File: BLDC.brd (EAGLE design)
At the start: 75.9 x 76.2 mm, 119 parts, among them J7 1-770178-0, J8 1-770174-1, U1 DRV8302, U102 LM3671MF-3.3/NOPB, U104 MCP2562, U2 STM32F405RGT6, Y1 8MHz

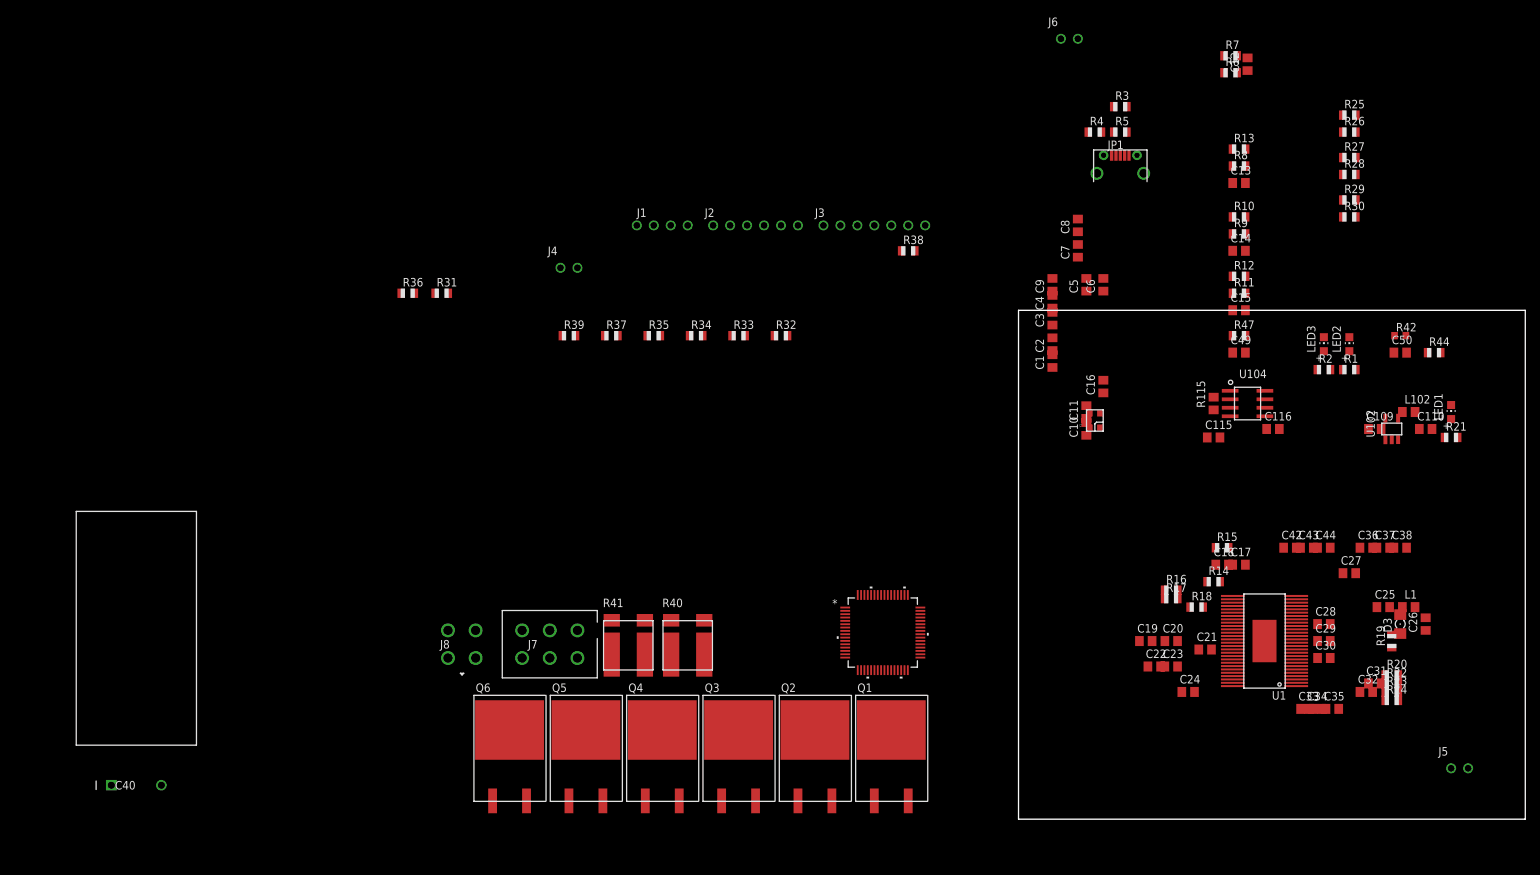
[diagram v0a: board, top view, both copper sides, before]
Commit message: renumbered parts
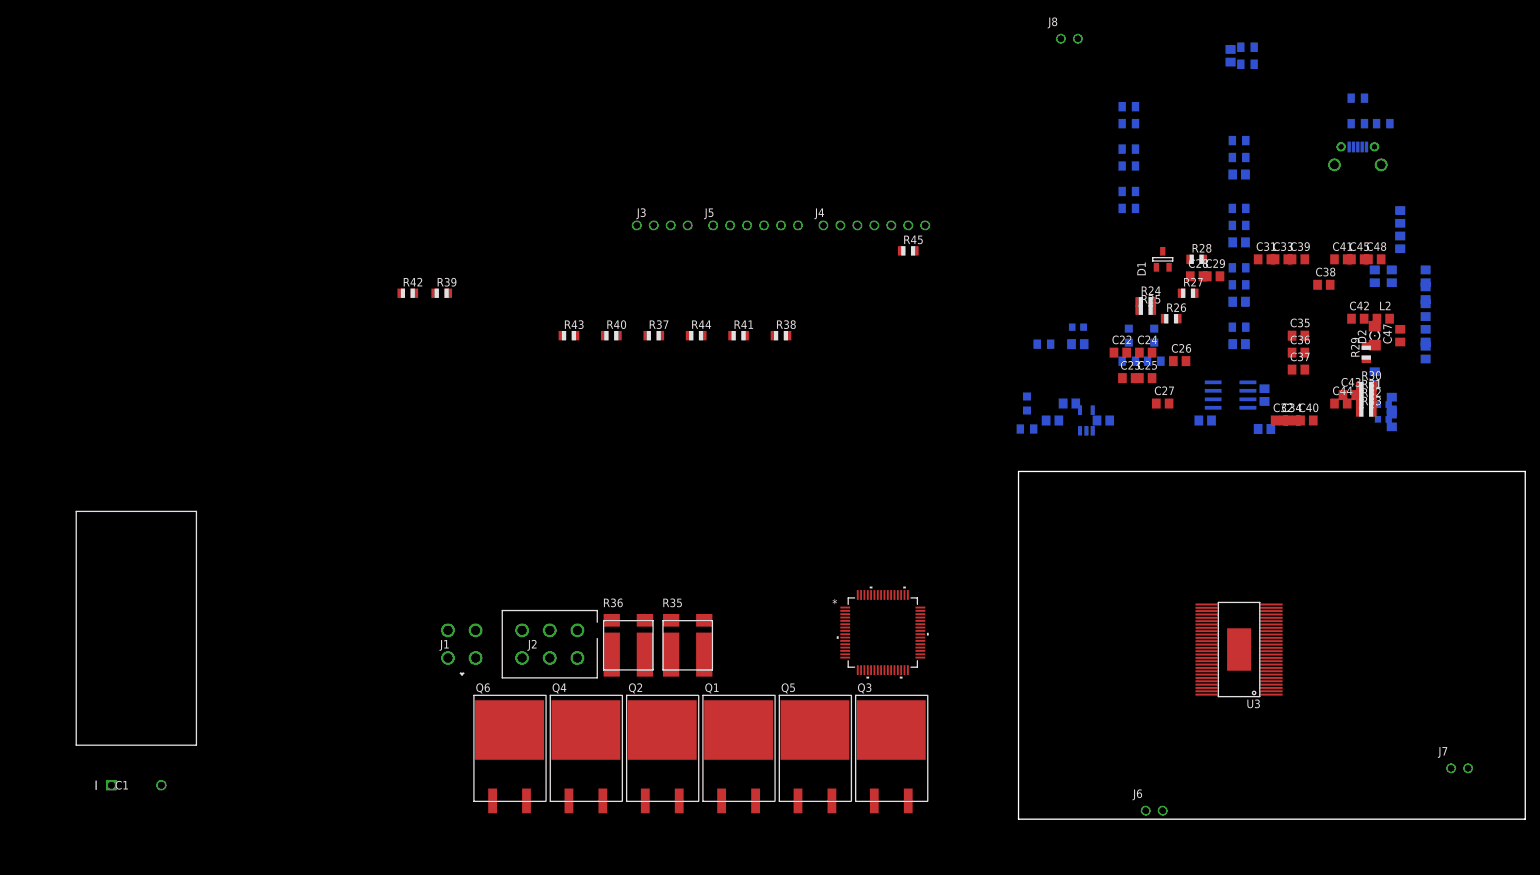
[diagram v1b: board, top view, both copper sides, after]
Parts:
- removed C109: 4.7uF, rcl:C0805
- removed C110: 10uF, rcl:C0805
- removed C115, C116: 0.1uF, rcl:C0805
- removed C49: 4n7, rcl:C0805
- removed C50: 2.2uf, rcl:C0805
- removed D3: (no value), FormE:1206-DIODE
- removed L102: 2.2uH, FormE:0805
- removed R115: 120R, rcl:R0805
- removed R47: 10K, adafruit:R0805
- removed U102: LM3671MF-3.3/NOPB, FormE:SOT23-5
- removed U104: MCP2562, FormE:SOIC8-N_MC
- added C39, C48: 15uf,100V, rcl:C0805
- added C41, C45: 10uf,50V, rcl:C0805
- added C46: 10uF, rcl:C0805
- added C47: 100uf, rcl:C0805
- added D1: 5V, FormE:SOT-23_DIODE
- added D2: (no value), FormE:1206-DIODE
- added L2: 2.2uH, FormE:0805
- added R43: 4.7R, adafruit:R0805
- added R45: 39k, adafruit:R0805
- added U3: DRV8302, FormE:HTSSOP-56
- added U4: LM3671MF-3.3/NOPB, FormE:SOT23-5
- C1: value 2.2uf -> 2200uF; device rcl:C0805 -> FormE:U1-PP-HORZ
- C11: value 15p -> 2.2uf
- C13, C14, C15: value 4n7 -> 2.2uf
- C17: value 120pf -> 2.2uf
- C18: value 6.8n -> 2.2uf
- C2, C7: value 2.2uf -> 0.1uF
- C21: value 22n -> 2.2uf
- C25: value 100n -> 2.2uf
- C26: value 100uf -> 22n
- C27: value 10uf, 50V -> 2.2uf
- C28: value 220n -> 6.8n
- C29: value 220n -> 120pf
- C3, C4, C5, C6: value 2.2uf -> 4n7
- C30: value 220n -> 4.7uF
- C31, C32: value 2.2n -> 10uf,50V
- C35, C36, C37: value 10uf,50V -> 220n
- C38: value 15uf,100V -> 10uf, 50V
- C40: value 2200uF -> 10uf,50V; device FormE:U1-PP-HORZ -> rcl:C0805
- C42: value 10uf,50V -> 100n
- C43: value 10uf,50V -> 2.2n
- C44: value 15uf,100V -> 2.2n
- C9: value 2.2uf -> 15p
- J1: value (none) -> 1-770174-1; device FormE:J_1X4 -> FormE:CON4_2X2_P163_VMNL-1MTG
- J2: value (none) -> 1-770178-0; device FormE:J_1X6 -> FormE:CON6_2X3_P163_VMNL-1MTG
- J3: device FormE:J_1X7 -> FormE:J_1X4
- J4: device FormE:J_1X2 -> FormE:J_1X7
- J5: device FormE:J_1X2 -> FormE:J_1X6
- J7: value 1-770178-0 -> (none); device FormE:CON6_2X3_P163_VMNL-1MTG -> FormE:J_1X2
- J8: value 1-770174-1 -> (none); device FormE:CON4_2X2_P163_VMNL-1MTG -> FormE:J_1X2
- R1: value 1k -> DNP
- R10, R26: value 2.2k -> 10k
- R12: value 2.2k -> 39K
- R14: value 220K -> 1k
- R15: value 15K -> 1k
- R16: value 18K -> 10K; device adafruit:R0805 -> FormE:0603
- R17: value 3K3 -> 10K
- R18: value 10k -> 39k
- R19: value 220K -> 2.2k
- R20, R22: value 100R -> 39k
- R21: value 1k -> 2.2k
- R23: value 100R -> 2.2k
- R24: value 100R -> 18K
- R25: value 39k -> 3K3
- R27, R29: value 39k -> 220K
- R28: value 2.2k -> 15K
- R30: value 2.2k -> 100R
- R31: value 39k -> 100R
- R32, R33: value 4.7R -> 100R
- R34: value 4.7R -> 1k
- R35: value 4.7R -> .001R; device adafruit:R0805 -> FormE:2726
- R36: value 39k -> .001R; device adafruit:R0805 -> FormE:2726
- R38: value 39k -> 4.7R
- R39: value 4.7R -> 39k
- R4: value 1k -> 120R; device adafruit:R0805 -> rcl:R0805
- R40, R41: value .001R -> 4.7R; device FormE:2726 -> adafruit:R0805
- R42: value 10K -> 39k; device FormE:0603 -> adafruit:R0805
- R44: value 10K -> 4.7R
- R5: value DNP -> 2.2k
- R7: value 39K -> 2.2k
- R8: value 10k -> 10K
- U1: value DRV8302 -> MCP2562; device FormE:HTSSOP-56 -> FormE:SOIC8-N_MC
- moved C40 183.6 mm to (43.2, 59.7)
- moved C1 151.1 mm to (-132.1, 5.08), turned to 0 degrees
- moved R42 148.7 mm to (-91.4, 78.7)
- moved R31 139.3 mm to (52.1, 63.5)
- moved J7 137.2 mm to (64.8, 7.62)
- moved J5 137.2 mm to (-45.7, 88.9)
- moved J8 127.6 mm to (6.35, 116.8)
- moved J6 116.3 mm to (19.1, 1.27)
- moved R44 110.5 mm to (-48.3, 72.4)
- moved R33 94.7 mm to (52.1, 61.0)
- moved R32 88.2 mm to (52.1, 62.2)
- moved R20 88.0 mm to (16.5, 100.3), flipped to the bottom
- moved R19 86.9 mm to (16.5, 104.1), flipped to the bottom, turned to 0 degrees
- moved R22 83.5 mm to (16.5, 94.0), flipped to the bottom
- moved R23 82.4 mm to (16.5, 91.4), flipped to the bottom
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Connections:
- net +3V3: now also C12.1, C13.1, C15.1, C16.1, C17.1, C20.1, C21.1, C46.1, J2.5, J4.P$6, L1.2, LED3.A, R16.2, R5.2, R6.2, R7.2, R8.2, U1.5, U3.24, U3.9, U4.4; no longer C1.1, C110.1, C115.1, C3.1, C4.1, C7.1, C8.1, C9.1, J3.P$6, J7.5, L102.2, LED1.A, R10.2, R12.2, R13.2, R42.2, R47.2, U1.24, U1.9, U102.4, U104.5
- net +5V: now also C30.1, C47.1, C7.1, D1.K, J3.P$4, J4.P$7, J5.P$6, L2.2, R1.1, R24.1, U1.3, U4.1, U4.3; no longer C109.1, C116.1, C26.1, J1.P$4, J2.P$6, J3.P$7, L1.2, R16.1, R5.1, U102.1, U102.3, U104.3
- net ADC_TEMP: now also C14.1, R16.1, R17.2; no longer C50.1, R42.1, R44.2
- net AN_IN: now also C8.1, R12.2, R13.1; no longer C12.1, R6.1, R7.2
- net AUX_1: now also J6.P$1; no longer J4.P$1
- net AUX_2: now also J6.P$2; no longer J4.P$2
- net AUX_3: now also J7.P$1; no longer J5.P$1
- net AUX_4: now also J7.P$2; no longer J5.P$2
- net AUX_5: now also J8.P$1; no longer J6.P$1
- net AUX_6: now also J8.P$2; no longer J6.P$2
- net BR_SO1: now also U3.25; no longer U1.25
- net BR_SO2: now also U3.26; no longer U1.26
- net CAR_CAN_N: now also J3.P$2, R4.1, U1.6; no longer J1.P$2, R115.1, U104.6
- net CAR_CAN_P: now also J3.P$3, R4.2, U1.7; no longer J1.P$3, R115.2, U104.7
- net CAR_CAN_RX: now also U1.4; no longer U104.4
- net CAR_CAN_TX: now also U1.1; no longer U104.1
- net DC_CAL: now also U3.12; no longer U1.12
- net DGND: now also C1.2; no longer C40.2
- net EN_GATE: now also U3.16; no longer U1.16
- net FAULT: now also U3.6; no longer U1.6
- net GND: now also C11.2, C21.2, C25.2, C28.2, C29.2, C30.2, C31.2, C32.2, C39.2, C40.2, C41.2, C45.2, C46.2, C47.2, C48.2, C9.1, D1.A, D2.A, J2.1, J4.P$1, J5.P$1, Q4.A2, R13.2, R14.1, R15.1, R17.1, R19.1, R23.1, R25.2, R27.2, R29.2, R34.1, R35.BL, R36.BL, R42.2, U1.2, U3.10, U3.28, U3.39, U3.57, U3.8, U4.2; no longer C1.2, C109.2, C11.1, C110.2, C115.2, C116.2, C26.2, C35.2, C36.2, C37.2, C42.2, C43.2, C44.2, C49.2, C50.2, C9.2, D3.A, J1.P$1, J2.P$1, J7.1, Q5.A2, R1.1, R14.2, R17.2, R18.1, R19.2, R2.1, R28.1, R30.1, R36.2, R40.BL, R41.BL, R44.1, R6.2, U1.10, U1.28, U1.39, U1.57, U102.2, U104.2, U104.8
- net H1: now also U3.17; no longer U1.17
- net H1_LOW: now also Q2.A2, R36.BR, R39.2, R42.1, U3.44; no longer Q4.A2, R31.2, R36.1, R41.BR, U1.44
- net H1_VS: now also C35.2, Q1.A2, Q2.K, R22.1, U3.46; no longer C28.2, Q3.A2, Q4.K, R29.1, U1.46
- net H2: now also U3.19; no longer U1.19
- net H2_VS: now also C36.2, Q3.A2, Q4.K, R20.1, U3.41; no longer C29.2, Q1.A2, Q5.K, R27.1, U1.41
- net H3: now also U3.21; no longer U1.21
- net H3_LOW: now also R35.BR, R45.2, U3.34; no longer R38.2, R40.BR, U1.34
- net H3_VS: now also C37.2, Q5.A2, R18.1, U3.36; no longer C30.2, Q2.A2, R25.1, U1.36
- net HALL_1_IN: now also J5.P$5, R5.1, R6.1, R7.1; no longer J2.P$5, R12.1, R13.1, R8.1
- net HALL_1_OUT: now also C3.1, C4.1, C5.1, R10.2; no longer C13.1, C14.1, C15.1, R8.2
- net HALL_2_IN: now also J5.P$4; no longer J2.P$4
- net HALL_3_IN: now also J5.P$3; no longer J2.P$3
- net L1: now also U3.18; no longer U1.18
- net L2: now also U3.20; no longer U1.20
- net L3: now also U3.22; no longer U1.22
- net LED_GREEN: now also LED1.A; no longer LED3.A
- net MISO_ADC_EXT2: now also J4.P$2; no longer J3.P$2
- net M_H1: now also R38.1, U3.47; no longer R32.1, U1.47
- net M_H2: now also R41.1, U3.42; no longer R33.1, U1.42
- net M_H3: now also R44.1, U3.37; no longer R34.1, U1.37
- net M_L1: now also R37.1, R43.1, U3.45; no longer R35.1, R39.1, U1.45
- net M_L2: now also R40.1, U3.40; no longer R37.1, U1.40
- net M_L3: now also U3.35; no longer U1.35
- net N$1: now also R15.2; no longer R1.2
- net N$10: now also C28.1, R28.1; no longer C18.1, R15.1
- net N$11: now also L1.1, U4.5; no longer L102.1, U102.5
- net N$12: now also C29.1, R28.2, U3.2; no longer C17.1, R15.2, U1.2
- net N$13: now also R24.2, R25.1, U3.3; no longer R16.2, R17.1, U1.3
- net N$14: now also R26.2, U3.7; no longer R18.2, U1.7
- net N$15: now also C25.1, U3.11, U3.23; no longer C22.1, U1.11, U1.23
- net N$16: now also C22.1, C24.1, U3.13; no longer C19.1, C20.1, U1.13
- net N$17: now also C26.1, U3.14; no longer C21.1, U1.14
- net N$18: now also C27.1, U3.27; no longer C24.1, U1.27
- net N$19: now also C26.2, U3.15; no longer C21.2, U1.15
- net N$2: now also LED1.C, R14.2; no longer LED3.C, R2.2
- net N$20: now also C42.1, U3.52; no longer C25.1, U1.52
- net N$21: now also C42.2, D2.C, L2.1, U3.50, U3.51; no longer C25.2, D3.C, L1.1, U1.50, U1.51
- net N$22: now also R29.1, U3.49; no longer R19.1, U1.49
- net N$23: now also C35.1, U3.48; no longer C28.1, U1.48
- net N$24: now also C43.1, R30.1, U3.33; no longer C31.1, R20.1, U1.33
- net N$25: now also C36.1, U3.43; no longer C29.1, U1.43
- net N$26: now also C43.2, R31.1, U3.32; no longer C31.2, R22.1, U1.32
- net N$27: now also C37.1, U3.38; no longer C30.1, U1.38
- net N$28: now also C44.2, R33.1, U3.30; no longer C32.2, R24.1, U1.30
- net N$29: now also C44.1, R32.1, U3.31; no longer C32.1, R23.1, U1.31
- net N$3: now also R3.2; no longer R4.2
- net N$30: now also Q1.A1, R38.2; no longer Q3.A1, R32.2
- net N$31: now also Q3.A1, R41.2; no longer Q1.A1, R33.2
- net N$32: now also Q5.A1, R44.2; no longer Q2.A1, R34.2
- net N$33: now also Q2.A1, R37.2, R39.1; no longer Q4.A1, R31.1, R35.2
- net N$34: now also Q4.A1, R40.2; no longer Q5.A1, R37.2
- net N$35: now also R43.2, R45.1; no longer R38.1, R39.2
- net N$4: now also R2.2; no longer R3.2
- net N$5: now also R1.2; no longer R5.2
- net N$6: now also C18.1, C19.1; no longer C5.1, C6.1
- net N$7: now also C10.2; no longer C11.2
- net N$8: now also C9.2; no longer C10.2
- net N$81: now also LED3.C, R34.2; no longer LED1.C, R21.2
- net N$9: now also R27.1, U3.1; no longer R14.1, U1.1
- net NRST: now also C11.1, J2.2; no longer C16.1, J7.2
- net RX_SCL_MOSI: now also J4.P$5; no longer J3.P$5
- net SCK_ADC_EXT: now also J4.P$3; no longer J3.P$3
- net SENS1: now also R18.2, R19.2; no longer R25.2, R26.2
- net SENS2: now also R20.2, R21.2; no longer R27.2, R28.2
- net SENS3: now also R22.2, R23.2; no longer R29.2, R30.2
- net SH1_A: now also R30.2, R35.TR; no longer R20.2, R40.TR
- net SH1_B: now also R31.2, R35.TL; no longer R22.2, R40.TL
- net SH2_A: now also R32.2, R36.TR; no longer R23.2, R41.TR
- net SH2_B: now also R33.2, R36.TL; no longer R24.2, R41.TL
- net SWCLK: now also J2.4; no longer J7.4
- net SWDIO: now also J2.3; no longer J7.3
- net TEMP_IN: now also J5.P$2, R8.1; no longer J2.P$2, R47.1
- net TEMP_MOTOR: now also C6.1; no longer C49.1
- net TX_SDA_NSS: now also J4.P$4; no longer J3.P$4
- net USB_DM: now also R3.1; no longer R4.1
- net USB_DP: now also R2.1; no longer R3.1
- net VCC: now also C1.1, C31.1, C32.1, C39.1, C41.1, C45.1, C48.1, Q5.K, U3.29, U3.53, U3.54; no longer C27.1, C35.1, C36.1, C37.1, C42.1, C43.1, C44.1, Q2.K, U1.29, U1.53, U1.54
- net V_BATT: now also R12.1; no longer R7.1
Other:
- board size 75.9 x 76.2 mm -> 75.9 x 52.1 mm

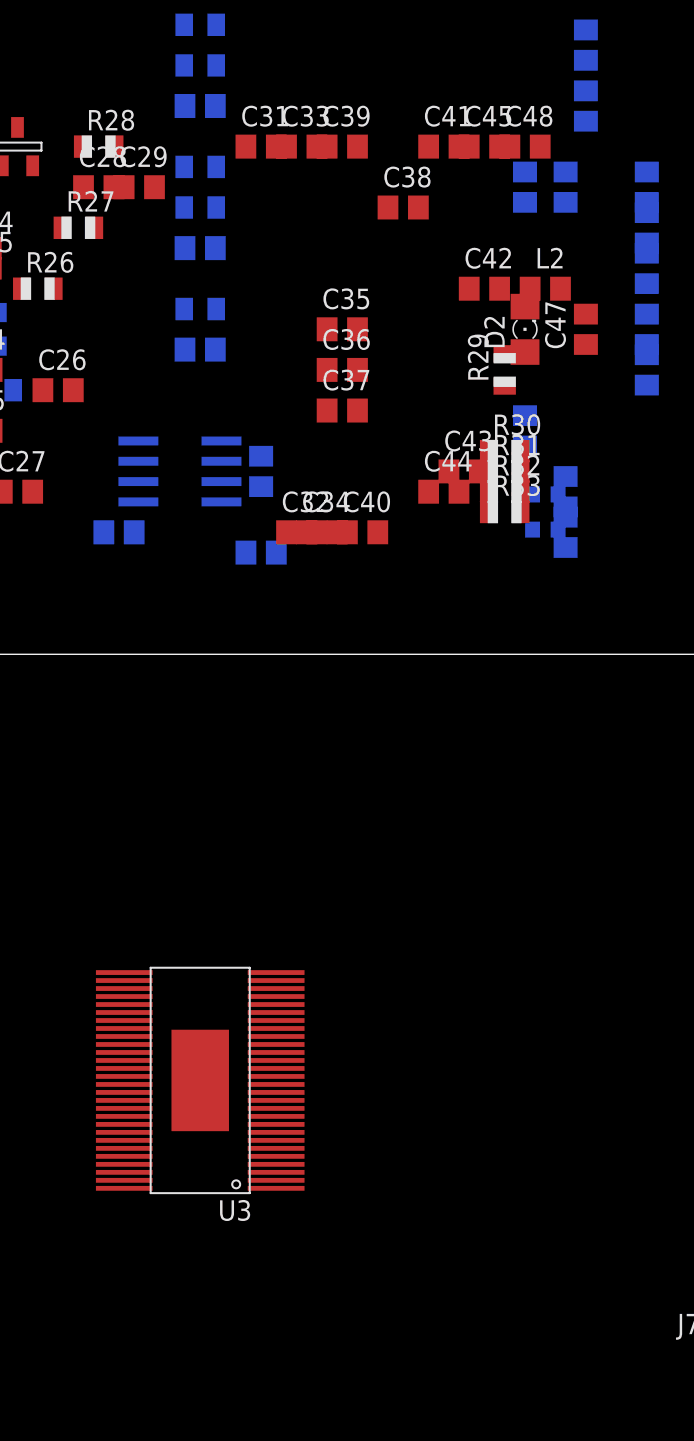
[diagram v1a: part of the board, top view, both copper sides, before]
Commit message: gate driver module progress
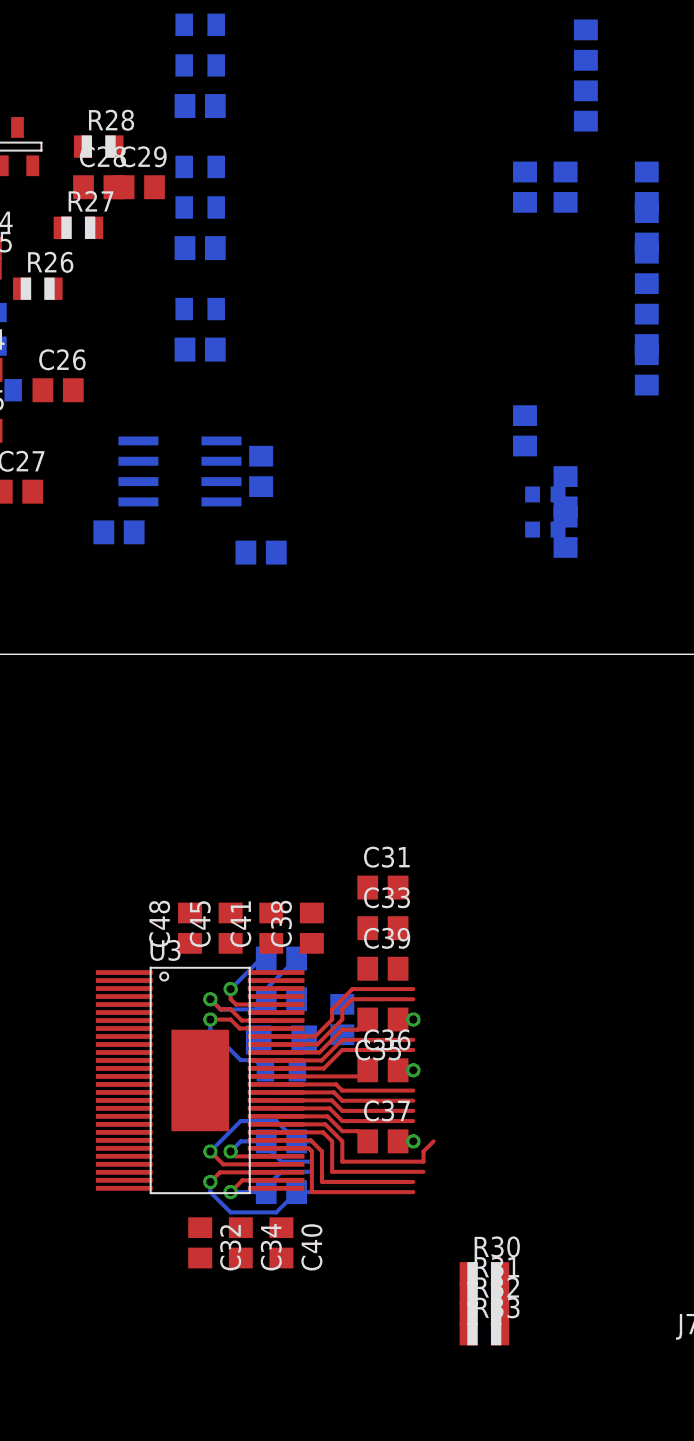
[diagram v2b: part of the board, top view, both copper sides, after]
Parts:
- moved C48 53.2 mm to (32.4, 34.9), turned to 90 degrees
- moved C39 51.5 mm to (44.5, 32.4)
- moved R31 51.5 mm to (50.8, 12.1)
- moved R33 51.5 mm to (50.8, 9.53)
- moved R30 51.5 mm to (50.8, 13.3)
- moved R32 51.5 mm to (50.8, 10.8)
- moved C45 51.4 mm to (34.9, 34.9), turned to 90 degrees
- moved C41 50.1 mm to (37.5, 34.9), turned to 90 degrees
- moved C33 49.2 mm to (44.5, 34.9)
- moved L2 47.4 mm to (38.1, 30.5), flipped to the bottom, turned to 180 degrees
- moved D2 47.0 mm to (38.1, 27.9), flipped to the bottom, turned to 180 degrees
- moved C31 47.0 mm to (44.5, 37.5)
- moved R29 46.0 mm to (38.1, 26.0), flipped to the bottom, turned to 180 degrees
- moved C47 45.8 mm to (41.9, 29.2), flipped to the bottom, turned to 270 degrees
- moved C37 45.8 mm to (44.5, 21.6)
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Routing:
- net M_H3: track 0.00 -> 12.5 mm
- net N$29: track 0.00 -> 12.4 mm, vias 0 -> 1
- net H3_VS: track 0.00 -> 12.3 mm, vias 0 -> 1
- net N$21: track 0.00 -> 12.2 mm, vias 0 -> 1
- net N$26: track 0.00 -> 12.1 mm, vias 0 -> 1
- net N$23: track 0.00 -> 11.4 mm, vias 0 -> 1
- net H3_LOW: track 0.00 -> 11.2 mm
- net M_L3: track 0.00 -> 10.8 mm
- net M_H1: track 0.00 -> 10.1 mm
- net H2_VS: track 0.00 -> 9.76 mm, vias 0 -> 1
- net N$22: track 0.00 -> 9.48 mm, vias 0 -> 1
- net M_L1: track 0.00 -> 9.12 mm
- net H1_LOW: track 0.00 -> 9.06 mm
- net N$24: track 0.00 -> 9.03 mm, vias 0 -> 1
- net N$28: track 0.00 -> 8.94 mm, vias 0 -> 1
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
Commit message: updated BOM
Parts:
- R8: value 10K -> 10k
- moved LED2 180.4 mm to (-147.3, -3.17), flipped to the top
